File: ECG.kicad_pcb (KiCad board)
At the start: 4 copper layers, 60 x 60 mm, 97 parts, among them J1 SJ-3566AN, J2 Conn_01x02_Male, J3 Conn_01x08_Male, J4 Conn_01x02_Male, J5 Conn_ARM_JTAG_SWD_10, Q1 BC858, U1 ADR4525, U2 LTC3531, U3 INA333, U4 OPA388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

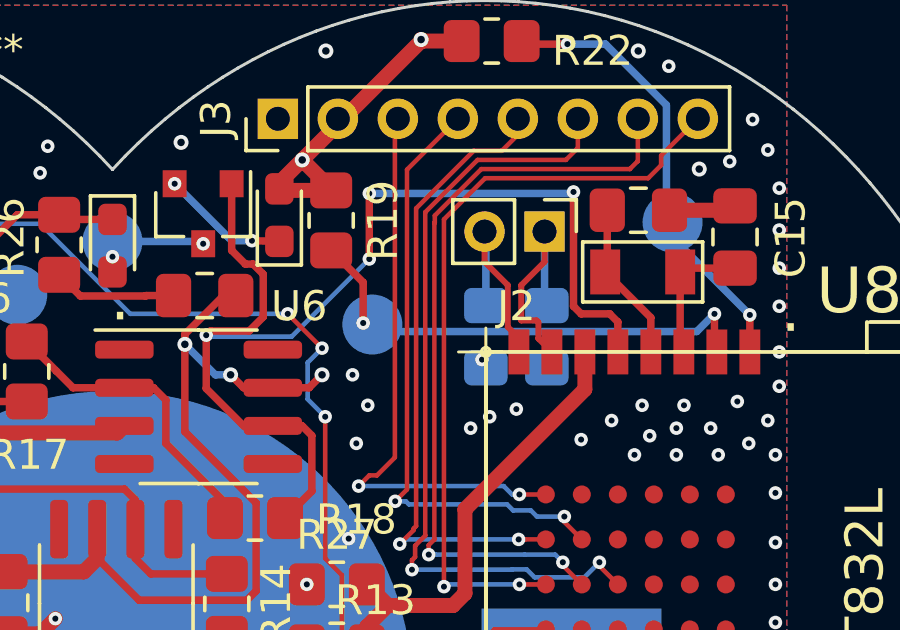
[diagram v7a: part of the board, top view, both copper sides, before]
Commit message: #27 - Fix gain stage clipping
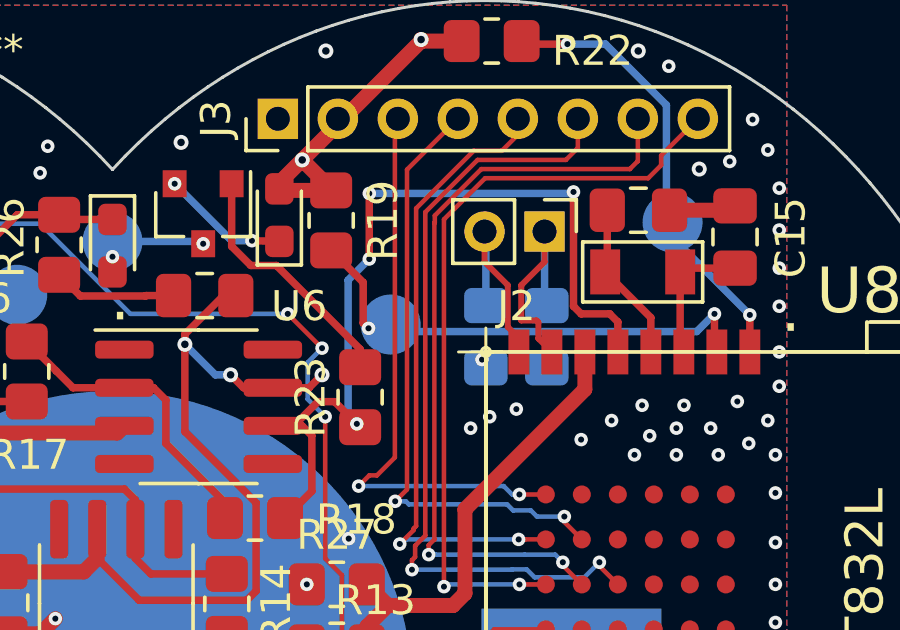
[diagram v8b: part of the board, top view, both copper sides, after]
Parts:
- added R23: 33k, Resistor_SMD:R_0805_2012Metric_Pad1.20x1.40mm_HandSolder, F.Cu at (160.0, 93.7)
- moved TP13 0.61 mm to (161.0, 91.3)
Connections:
- Q1 pad 1: Signal -> Net-(Q1-Pad1)
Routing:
- net Signal: track 38.3 -> 29.6 mm
- net Net-(Q1-Pad1): track 0.00 -> 8.39 mm
- net GND: vias 208 -> 205
